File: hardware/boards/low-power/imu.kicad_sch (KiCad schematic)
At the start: 3 parts, among them U3 LSM6DSM

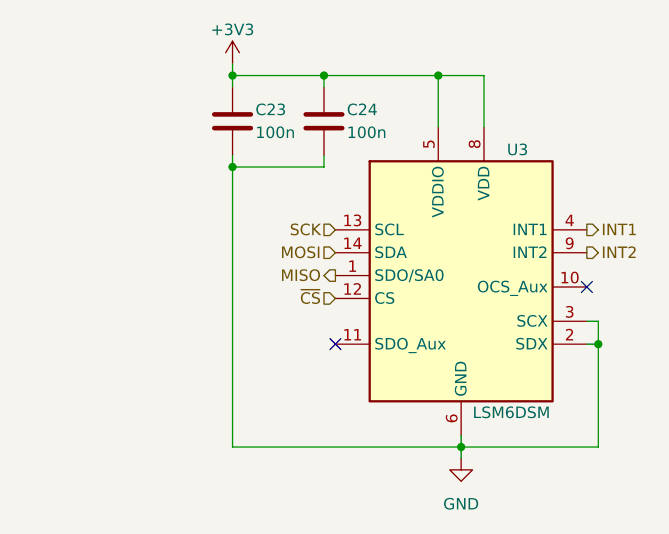
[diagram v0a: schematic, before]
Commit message: Add footprints and models for LP board
Also completed rough layout for LP board to estimate board space usage.
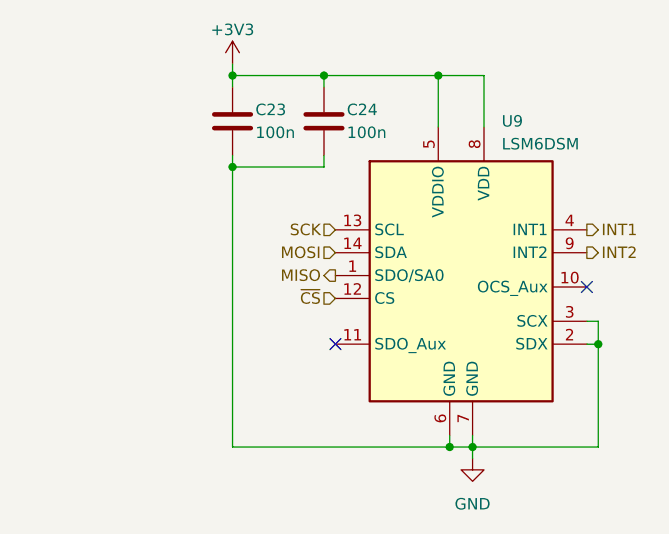
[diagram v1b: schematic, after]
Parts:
- removed U3: LSM6DSM, Package_LGA:LGA-14_3x2.5mm_P0.5mm_LayoutBorder3x4y, symbol Capstone:LSM6DSM
- added U9: LSM6DSM, Package_LGA:LGA-14_3x2.5mm_P0.5mm_LayoutBorder3x4y, symbol Capstone:LSM6DSM
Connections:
- net +3V3: now also U9.5 (VDDIO), U9.8 (VDD)
- net GND: now also U9.2 (SDX), U9.3 (SCX), U9.6 (GND), U9.7 (GND)
- net INT1: now also U9.4 (INT1)
- net INT2: now also U9.9 (INT2)
- net MISO: now also U9.1 (SDO/SA0)
- net MOSI: now also U9.14 (SDA)
- net SCK: now also U9.13 (SCL)
- net ~{CS}: now also U9.12 (CS)
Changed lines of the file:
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@@
   (junction (at 123.19 77.47) (diameter 0) (color 0 0 0 0)
   )
+  (junction (at 147.32 118.745) (diameter 0) (color 0 0 0 0)
+  )
   (junction (at 163.83 107.315) (diameter 0) (color 0 0 0 0)
   )
+  (junction (at 149.86 118.745) (diameter 0) (color 0 0 0 0)
+  )
   (junction (at 146.05 77.47) (diameter 0) (color 0 0 0 0)
-  )
-  (junction (at 148.59 118.745) (diameter 0) (color 0 0 0 0)
   )
   (junction (at 123.19 87.63) (diameter 0) (color 0 0 0 0)
@@
     (stroke (width 0) (type default))
   )
+  (wire (pts (xy 147.32 118.745) (xy 149.86 118.745))
+    (stroke (width 0) (type default))
+  )
   (wire (pts (xy 123.19 87.63) (xy 123.19 118.745))
     (stroke (width 0) (type default))
@@
     (stroke (width 0) (type default))
   )
+  (wire (pts (xy 149.86 117.475) (xy 149.86 118.745))
+    (stroke (width 0) (type default))
+  )
   (wire (pts (xy 123.19 86.36) (xy 123.19 87.63))
     (stroke (width 0) (type default))
@@
     (stroke (width 0) (type default))
   )
-  (wire (pts (xy 123.19 118.745) (xy 148.59 118.745))
+  (wire (pts (xy 123.19 118.745) (xy 147.32 118.745))
     (stroke (width 0) (type default))
   )
@@
     (stroke (width 0) (type default))
   )
-  (wire (pts (xy 148.59 117.475) (xy 148.59 118.745))
-    (stroke (width 0) (type default))
-  )
   (wire (pts (xy 163.83 107.315) (xy 162.56 107.315))
     (stroke (width 0) (type default))
@@
     (stroke (width 0) (type default))
   )
-  (wire (pts (xy 148.59 118.745) (xy 163.83 118.745))
-    (stroke (width 0) (type default))
-  )
   (wire (pts (xy 162.56 104.775) (xy 163.83 104.775))
     (stroke (width 0) (type default))
   )
-  (wire (pts (xy 148.59 118.745) (xy 148.59 120.015))
+  (wire (pts (xy 149.86 118.745) (xy 163.83 118.745))
+    (stroke (width 0) (type default))
+  )
+  (wire (pts (xy 147.32 117.475) (xy 147.32 118.745))
+    (stroke (width 0) (type default))
+  )
+  (wire (pts (xy 149.86 118.745) (xy 149.86 120.015))
     (stroke (width 0) (type default))
   )
@@
     (effects (font (size 1.27 1.27)) (justify right))
   )
-  (symbol (lib_id "power:GND") (at 148.59 120.015 0) (unit 1)
+  (symbol (lib_id "power:GND") (at 149.86 120.015 0) (unit 1)
     (in_bom yes) (on_board yes) (dnp no) (fields_autoplaced)
-    (property "Reference" "#PWR012" (at 148.59 126.365 0)
-      (effects (font (size 1.27 1.27)) hide)
-    )
-    (property "Value" "GND" (at 148.59 125.095 0)
+    (property "Reference" "#PWR012" (at 149.86 126.365 0)
+      (effects (font (size 1.27 1.27)) hide)
+    )
+    (property "Value" "GND" (at 149.86 125.095 0)
       (effects (font (size 1.27 1.27)))
     )
-    (property "Footprint" "" (at 148.59 120.015 0)
-      (effects (font (size 1.27 1.27)) hide)
-    )
-    (property "Datasheet" "" (at 148.59 120.015 0)
+    (property "Footprint" "" (at 149.86 120.015 0)
+      (effects (font (size 1.27 1.27)) hide)
+    )
+    (property "Datasheet" "" (at 149.86 120.015 0)
       (effects (font (size 1.27 1.27)) hide)
     )
@@
   )
   (symbol (lib_id "Capstone:LSM6DSM") (at 149.86 98.425 0) (unit 1)
-    (in_bom yes) (on_board yes) (dnp no)
-    (property "Reference" "U3" (at 153.67 85.725 0)
-      (effects (font (size 1.27 1.27)) (justify left))
-    )
-    (property "Value" "LSM6DSM" (at 149.86 114.935 0)
+    (in_bom yes) (on_board yes) (dnp no) (fields_autoplaced)
+    (property "Reference" "U9" (at 153.0859 82.55 0)
+      (effects (font (size 1.27 1.27)) (justify left))
+    )
+    (property "Value" "LSM6DSM" (at 153.0859 85.09 0)
       (effects (font (size 1.27 1.27)) (justify left))
     )
@@
     (pin "5")
     (pin "6")
+    (pin "7")
     (pin "8")
     (pin "9")
     (instances
       (project "low-power"
-        (path "/71f6a5b4-1ac6-435b-9486-30b16ab86e62"
-          (reference "U3") (unit 1)
-        )
         (path "/71f6a5b4-1ac6-435b-9486-30b16ab86e62/46cd4623-be7a-4a19-9b38-60ae4f389fe5"
           (reference "U9") (unit 1)

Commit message: Add initial changes after schematic review
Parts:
- added R701: 100k, Resistor_SMD:R_0201_0603Metric, symbol Device:R
- renumbered U9 to U701
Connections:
- net GND: now also R701.2
- net ~{CS}: now also R701.1
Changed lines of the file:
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@@
   (junction (at 146.05 77.47) (diameter 0) (color 0 0 0 0)
   )
+  (junction (at 128.905 118.745) (diameter 0) (color 0 0 0 0)
+  )
   (junction (at 123.19 87.63) (diameter 0) (color 0 0 0 0)
+  )
+  (junction (at 128.905 102.235) (diameter 0) (color 0 0 0 0)
   )
   (junction (at 133.35 77.47) (diameter 0) (color 0 0 0 0)
@@
     (stroke (width 0) (type default))
   )
+  (wire (pts (xy 107.95 102.235) (xy 128.905 102.235))
+    (stroke (width 0) (type default))
+  )
   (wire (pts (xy 147.32 118.745) (xy 149.86 118.745))
     (stroke (width 0) (type default))
@@
     (stroke (width 0) (type default))
   )
+  (wire (pts (xy 128.905 115.57) (xy 128.905 118.745))
+    (stroke (width 0) (type default))
+  )
+  (wire (pts (xy 128.905 102.235) (xy 128.905 107.95))
+    (stroke (width 0) (type default))
+  )
   (wire (pts (xy 123.19 86.36) (xy 123.19 87.63))
     (stroke (width 0) (type default))
@@
     (stroke (width 0) (type default))
   )
-  (wire (pts (xy 123.19 118.745) (xy 147.32 118.745))
+  (wire (pts (xy 123.19 118.745) (xy 128.905 118.745))
     (stroke (width 0) (type default))
   )
@@
     (stroke (width 0) (type default))
   )
+  (wire (pts (xy 128.905 118.745) (xy 147.32 118.745))
+    (stroke (width 0) (type default))
+  )
   (wire (pts (xy 163.83 107.315) (xy 162.56 107.315))
     (stroke (width 0) (type default))
@@
   )
   (wire (pts (xy 133.35 87.63) (xy 133.35 86.36))
+    (stroke (width 0) (type default))
+  )
+  (wire (pts (xy 128.905 102.235) (xy 134.62 102.235))
     (stroke (width 0) (type default))
   )
@@
     (effects (font (size 1.27 1.27)) (justify left))
   )
-  (hierarchical_label "~{CS}" (shape input) (at 134.62 102.235 180) (fields_autoplaced)
+  (hierarchical_label "~{CS}" (shape input) (at 107.95 102.235 180) (fields_autoplaced)
     (effects (font (size 1.27 1.27)) (justify right))
   )
@@
         )
         (path "/71f6a5b4-1ac6-435b-9486-30b16ab86e62/46cd4623-be7a-4a19-9b38-60ae4f389fe5"
-          (reference "#PWR048") (unit 1)
+          (reference "#PWR0702") (unit 1)
         )
       )
@@
         )
         (path "/71f6a5b4-1ac6-435b-9486-30b16ab86e62/46cd4623-be7a-4a19-9b38-60ae4f389fe5"
-          (reference "C48") (unit 1)
+          (reference "C701") (unit 1)
         )
       )
@@
         )
         (path "/71f6a5b4-1ac6-435b-9486-30b16ab86e62/46cd4623-be7a-4a19-9b38-60ae4f389fe5"
-          (reference "C49") (unit 1)
+          (reference "C702") (unit 1)
+        )
+      )
+    )
+  )
+  (symbol (lib_id "Device:R") (at 128.905 111.76 0) (unit 1)
+    (in_bom yes) (on_board yes) (dnp no) (fields_autoplaced)
+    (property "Reference" "R701" (at 130.81 111.125 0)
+      (effects (font (size 1.27 1.27)) (justify left))
+    )
+    (property "Value" "100k" (at 130.81 113.665 0)
+      (effects (font (size 1.27 1.27)) (justify left))
+    )
+    (property "Footprint" "Resistor_SMD:R_0201_0603Metric" (at 127.127 111.76 90)
+      (effects (font (size 1.27 1.27)) hide)
+    )
+    (property "Datasheet" "~" (at 128.905 111.76 0)
+      (effects (font (size 1.27 1.27)) hide)
+    )
+    (pin "1")
+    (pin "2")
+    (instances
+      (project "low-power"
+        (path "/71f6a5b4-1ac6-435b-9486-30b16ab86e62/46cd4623-be7a-4a19-9b38-60ae4f389fe5"
+          (reference "R701") (unit 1)
         )
       )
@@
         )
         (path "/71f6a5b4-1ac6-435b-9486-30b16ab86e62/46cd4623-be7a-4a19-9b38-60ae4f389fe5"
-          (reference "#PWR047") (unit 1)
+          (reference "#PWR0701") (unit 1)
         )
       )
@@
   (symbol (lib_id "Capstone:LSM6DSM") (at 149.86 98.425 0) (unit 1)
     (in_bom yes) (on_board yes) (dnp no) (fields_autoplaced)
-    (property "Reference" "U9" (at 153.0859 82.55 0)
+    (property "Reference" "U701" (at 153.0859 82.55 0)
       (effects (font (size 1.27 1.27)) (justify left))
     )
@@
       (project "low-power"
         (path "/71f6a5b4-1ac6-435b-9486-30b16ab86e62/46cd4623-be7a-4a19-9b38-60ae4f389fe5"
-          (reference "U9") (unit 1)
-        )
-      )
+          (reference "U701") (unit 1)
+        )
+      )
